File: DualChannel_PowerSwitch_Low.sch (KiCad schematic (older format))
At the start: 14 parts, among them J1 Conn_01x04, J2 Conn_01x04, M1 SCREW_6-32_POWER, M2 SCREW_6-32_POWER, M4 SCREW_6-32_POWER, M5 SCREW_6-32_POWER, M6 SCREW_6-32_POWER, M7 SCREW_6-32_POWER, Q1 INFINEON_IRLML0040TRPBF, Q2 INFINEON_IRLML0040TRPBF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

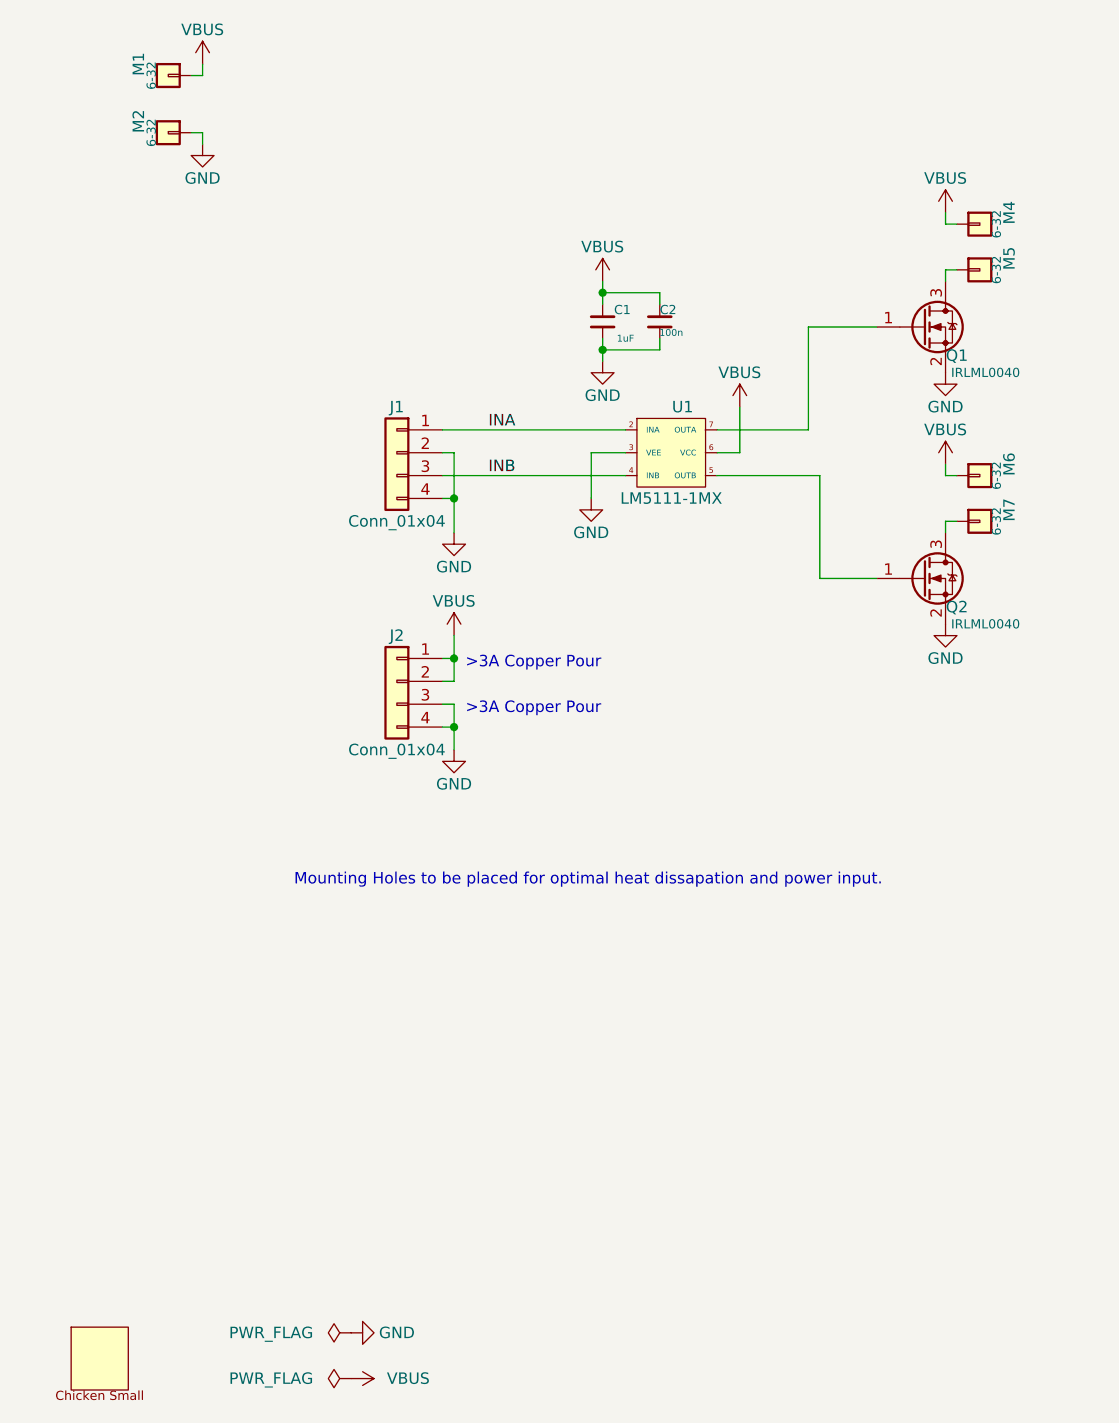
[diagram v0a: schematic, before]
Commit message: Adjusted header position slightly
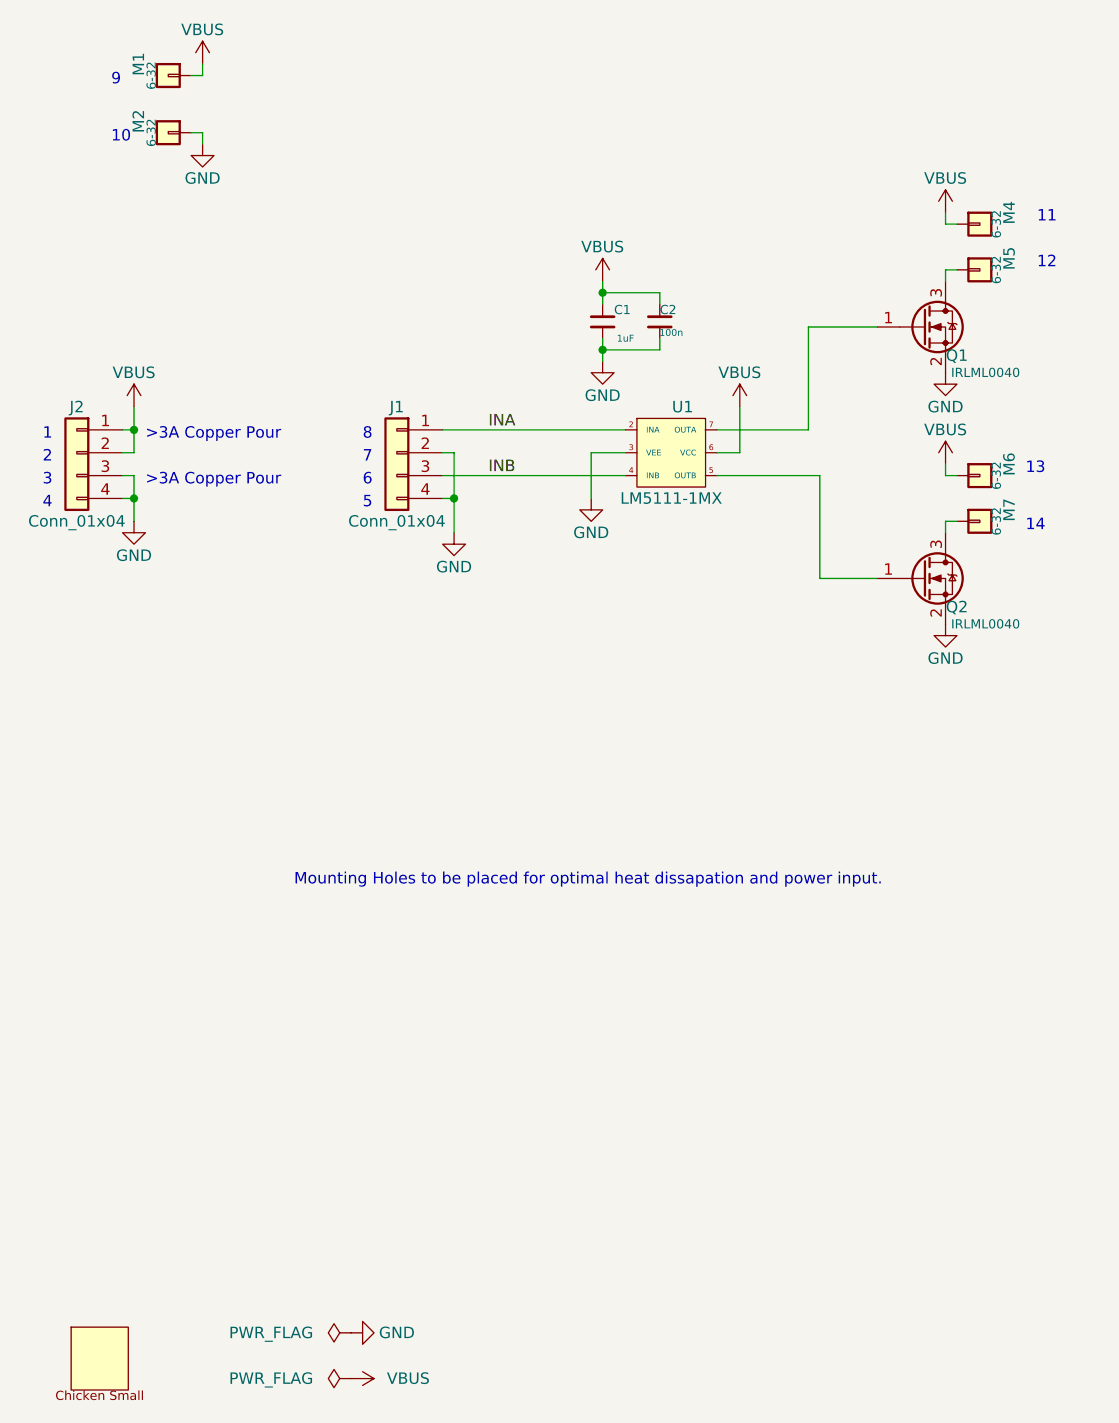
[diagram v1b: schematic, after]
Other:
- note added: "1"
- note added: "10"
- note added: "11"
- note added: "12"
- note added: "13"
- note added: "14"
- note added: "2"
- note added: "3"
- note added: "4"
- note added: "5"
- note added: "6"
- note added: "7"
- note added: "8"
- note added: "9"
- moved on the sheet: J2
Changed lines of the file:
@@
 L Connector_Generic:Conn_01x04 J2
 U 1 1 616ADEEC
-P 3400 3850
-F 0 "J2" H 3400 4050 50  0000 C CNN
-F 1 "Conn_01x04" H 3400 3550 50  0000 C CNN
-F 2 "Pin_Headers:Pin_Header_Straight_1x04_Pitch2.54mm" H 3400 3850 50  0001 C CNN
-F 3 "~" H 3400 3850 50  0001 C CNN
-	1    3400 3850
+P 2000 2850
+F 0 "J2" H 2000 3050 50  0000 C CNN
+F 1 "Conn_01x04" H 2000 2550 50  0000 C CNN
+F 2 "Pin_Headers:Pin_Header_Straight_1x04_Pitch2.54mm" H 2000 2850 50  0001 C CNN
+F 3 "~" H 2000 2850 50  0001 C CNN
+	1    2000 2850
 	-1   0    0    -1
 $EndComp
@@
 L power:VBUS #PWR05
 U 1 1 616AE9B3
-P 3650 3650
-F 0 "#PWR05" H 3650 3500 50  0001 C CNN
-F 1 "VBUS" H 3650 3800 50  0000 C CNN
-F 2 "" H 3650 3650 50  0001 C CNN
-F 3 "" H 3650 3650 50  0001 C CNN
-	1    3650 3650
-	1    0    0    -1
-$EndComp
-Wire Wire Line
-	3600 3850 3650 3850
-Wire Wire Line
-	3650 3850 3650 3750
-Wire Wire Line
-	3600 3750 3650 3750
-Connection ~ 3650 3750
-Wire Wire Line
-	3650 3750 3650 3650
+P 2250 2650
+F 0 "#PWR05" H 2250 2500 50  0001 C CNN
+F 1 "VBUS" H 2250 2800 50  0000 C CNN
+F 2 "" H 2250 2650 50  0001 C CNN
+F 3 "" H 2250 2650 50  0001 C CNN
+	1    2250 2650
+	1    0    0    -1
+$EndComp
+Wire Wire Line
+	2200 2850 2250 2850
+Wire Wire Line
+	2250 2850 2250 2750
+Wire Wire Line
+	2200 2750 2250 2750
+Connection ~ 2250 2750
+Wire Wire Line
+	2250 2750 2250 2650
 $Comp
 L power:GND #PWR06
 U 1 1 616AF991
-P 3650 4150
-F 0 "#PWR06" H 3650 3900 50  0001 C CNN
-F 1 "GND" H 3650 4000 50  0000 C CNN
-F 2 "" H 3650 4150 50  0001 C CNN
-F 3 "" H 3650 4150 50  0001 C CNN
-	1    3650 4150
-	1    0    0    -1
-$EndComp
-Wire Wire Line
-	3650 4150 3650 4050
-Wire Wire Line
-	3650 3950 3600 3950
-Wire Wire Line
-	3600 4050 3650 4050
-Connection ~ 3650 4050
-Wire Wire Line
-	3650 4050 3650 3950
-Text Notes 3700 3800 0    50   ~ 0
+P 2250 3150
+F 0 "#PWR06" H 2250 2900 50  0001 C CNN
+F 1 "GND" H 2250 3000 50  0000 C CNN
+F 2 "" H 2250 3150 50  0001 C CNN
+F 3 "" H 2250 3150 50  0001 C CNN
+	1    2250 3150
+	1    0    0    -1
+$EndComp
+Wire Wire Line
+	2250 3150 2250 3050
+Wire Wire Line
+	2250 2950 2200 2950
+Wire Wire Line
+	2200 3050 2250 3050
+Connection ~ 2250 3050
+Wire Wire Line
+	2250 3050 2250 2950
+Text Notes 2300 2800 0    50   ~ 0
 >3A Copper Pour
-Text Notes 3700 4000 0    50   ~ 0
+Text Notes 2300 3000 0    50   ~ 0
 >3A Copper Pour
 $Comp
@@
 	1    0    0    -1
 $EndComp
+Text Notes 1850 2800 0    50   ~ 0
+1
+Text Notes 1850 2900 0    50   ~ 0
+2
+Text Notes 1850 3000 0    50   ~ 0
+3
+Text Notes 1850 3100 0    50   ~ 0
+4
+Text Notes 3250 3100 0    50   ~ 0
+5
+Text Notes 3250 3000 0    50   ~ 0
+6
+Text Notes 3250 2900 0    50   ~ 0
+7
+Text Notes 3250 2800 0    50   ~ 0
+8
+Text Notes 2150 1250 0    50   ~ 0
+9
+Text Notes 2150 1500 0    50   ~ 0
+10
+Text Notes 6200 1850 0    50   ~ 0
+11
+Text Notes 6200 2050 0    50   ~ 0
+12
+Text Notes 6150 2950 0    50   ~ 0
+13
+Text Notes 6150 3200 0    50   ~ 0
+14
 $EndSCHEMATC
